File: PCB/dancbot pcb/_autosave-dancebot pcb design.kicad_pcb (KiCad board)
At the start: 2 copper layers, 62 x 54 mm, 27 parts, among them J1 ESP32-PICO-KIT-V4.1, J2 Voltage Regulator, J4 Pins, J6 Conn_01x04_Socket, J7 Conn_01x04_Socket, Q1 PMOS, Q2 PMOS, Q3 2N3904, Q5 PMOS, SW1 SP switch, SW2 SW_SPST

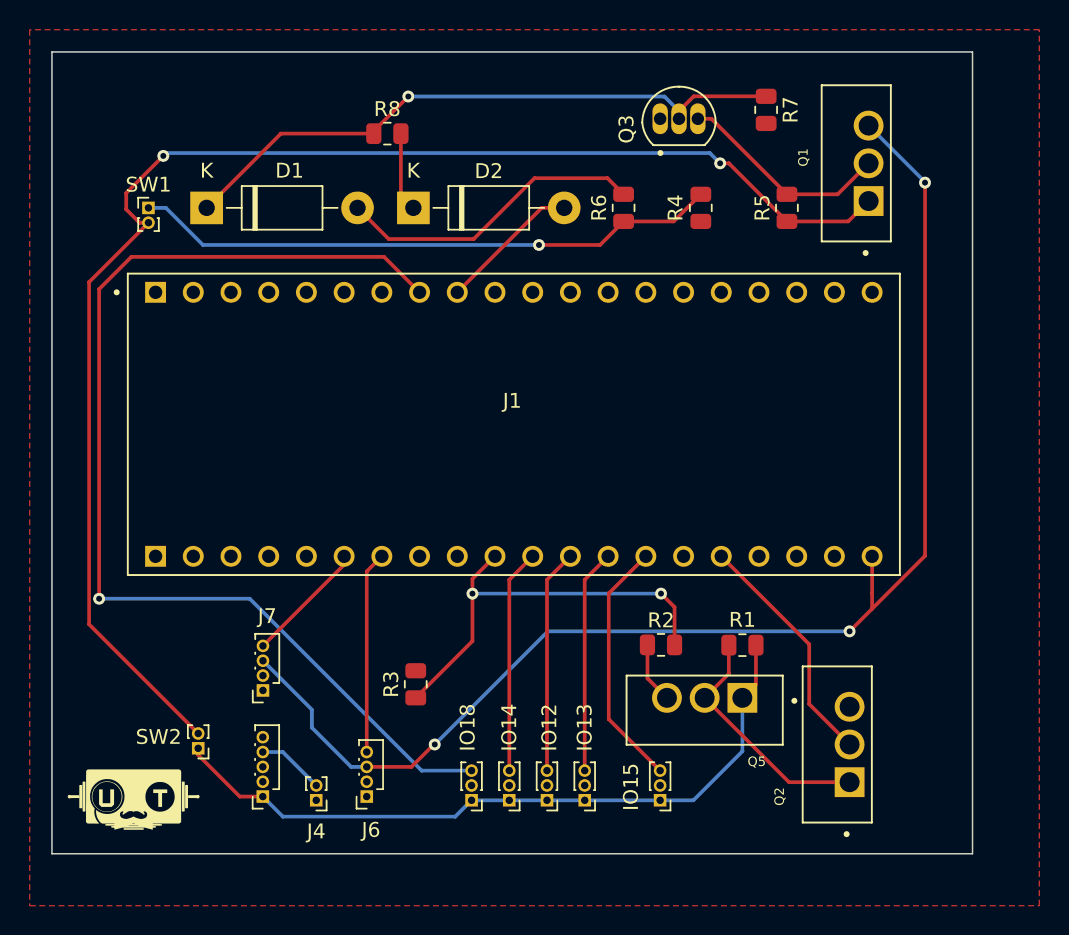
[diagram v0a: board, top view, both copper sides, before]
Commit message: Routing rev 6, trace width increased, smd components added
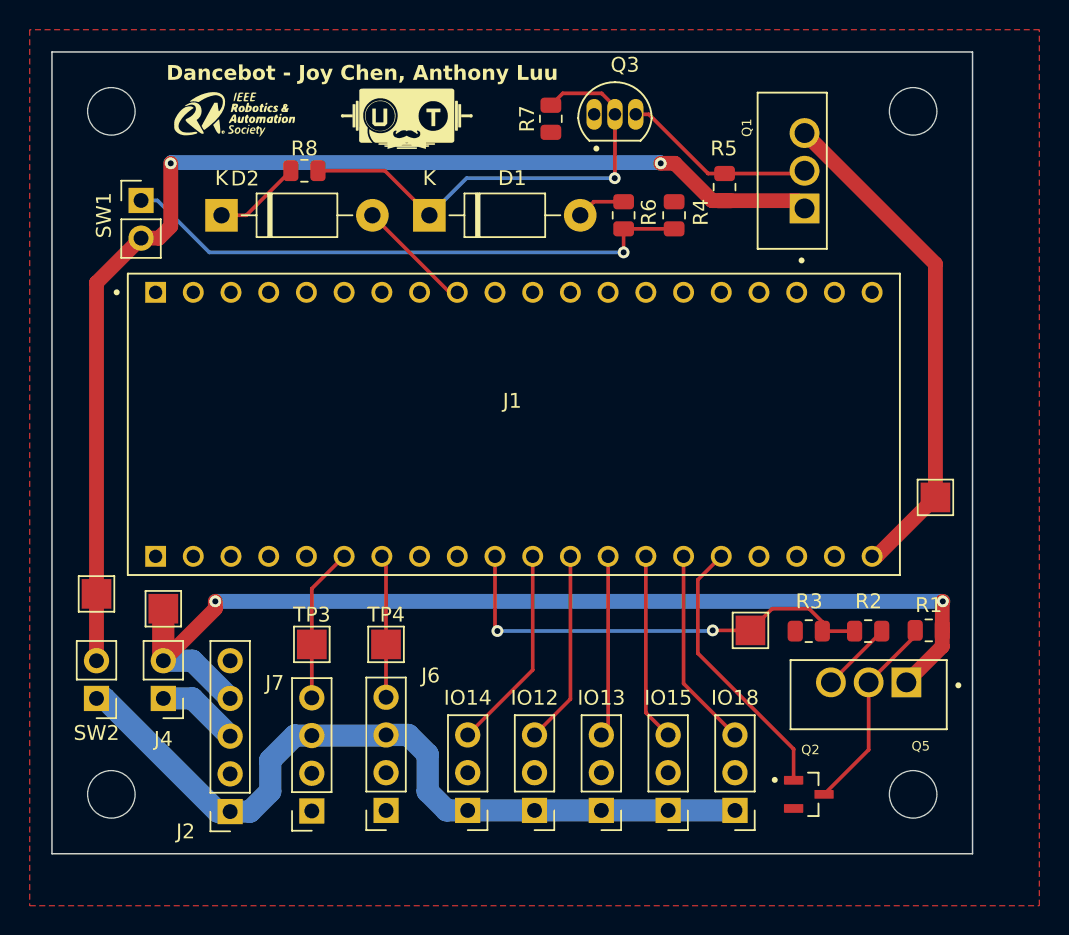
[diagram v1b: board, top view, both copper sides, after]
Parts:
- added G***: LOGO, LOGO, F.Cu at (194.8, 61.7)
- added H1: MountingHole, MountingHole:MountingHole_3.2mm_M3, F.Cu at (186.5, 61.5)
- added H2: MountingHole, MountingHole:MountingHole_3.2mm_M3, F.Cu at (240.5, 61.5)
- added H3: MountingHole, MountingHole:MountingHole_3.2mm_M3, F.Cu at (186.5, 107.5)
- added H4: MountingHole, MountingHole:MountingHole_3.2mm_M3, F.Cu at (240.5, 107.5)
- added TP1: TestPoint, TestPoint:TestPoint_Pad_2.0x2.0mm, F.Cu at (185.5, 94.0)
- added TP2: TestPoint, TestPoint:TestPoint_Pad_2.0x2.0mm, F.Cu at (242.0, 87.5)
- added TP3: TestPoint, TestPoint:TestPoint_Pad_2.0x2.0mm, F.Cu at (200.0, 97.4)
- added TP4: TestPoint, TestPoint:TestPoint_Pad_2.0x2.0mm, F.Cu at (205.0, 97.4)
- added TP5: TestPoint, TestPoint:TestPoint_Pad_2.0x2.0mm, F.Cu at (190.0, 95.0)
- added TP9: TestPoint, TestPoint:TestPoint_Pad_2.0x2.0mm, F.Cu at (229.5, 96.5)
- IO12, IO13, IO14, IO15, IO18: footprint Connector_PinHeader_1.00mm:PinHeader_1x03_P1.00mm_Vertical -> Connector_PinHeader_2.54mm:PinHeader_1x03_P2.54mm_Vertical
- J2: footprint Connector_PinSocket_1.00mm:PinSocket_1x05_P1.00mm_Vertical -> Connector_PinSocket_2.54mm:PinSocket_1x05_P2.54mm_Vertical
- J4, SW1, SW2: footprint Connector_PinHeader_1.00mm:PinHeader_1x02_P1.00mm_Vertical -> Connector_PinHeader_2.54mm:PinHeader_1x02_P2.54mm_Vertical
- J6, J7: footprint Connector_PinSocket_1.00mm:PinSocket_1x04_P1.00mm_Vertical -> Connector_PinSocket_2.54mm:PinSocket_1x04_P2.54mm_Vertical
- Q2: value PMOS -> NMOS; footprint dancebot pcb libraries stuff:TO254P1052X465X1989-3 -> Dancebot Footprints:SOT95P237X112-3N
- Q3: footprint 2N3904:TO92127P495H495-3 -> Dancebot Footprints:TO92127P495H495-3
- Q5: footprint dancebot pcb libraries stuff:TO254P1052X465X1989-3 -> Dancebot Footprints:TO254P1052X465X1989-3
- R3: value 10K -> 51k
- moved G*** 49.4 mm to (206.4, 61.6)
- moved R3 26.7 mm to (233.5, 96.5), turned to 180 degrees
- moved IO18 17.8 mm to (228.5, 108.6)
- moved D1 15.0 mm to (207.9, 68.5)
- moved R7 14.5 mm to (216.1, 62.0)
- moved R2 14.0 mm to (237.5, 96.5), turned to 180 degrees
- moved D2 12.9 mm to (193.9, 68.5)
- moved R1 12.6 mm to (241.6, 96.5)
- moved J4 12.4 mm to (190.0, 101.0)
- moved Q5 11.1 mm to (240.0, 100.0)
- moved J7 8.76 mm to (200.0, 108.6)
- moved SW2 7.63 mm to (185.5, 101.0)
- moved R8 6.12 mm to (199.5, 65.5), turned to 180 degrees
- moved R5 4.43 mm to (227.8, 66.6)
- moved Q1 4.34 mm to (233.2, 68.0)
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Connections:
- J1 pad J2_8: SM5 -> unconnected-(J1-IO18-PadJ2_8)
- J1 pad J3_15: unconnected-(J1-IO2-PadJ3_15) -> SM5
- J4 pad 1: GND1 -> Batt GND
- J6 pad 3: +5V -> VOUT
- J7 pad 3: +5V -> VOUT
- Q2 pad 1: Net-(Q2-D) -> BATT EN
- Q2 pad 2: BATT EN -> GND1
- Q2 pad 3: GND1 -> Net-(Q5-G)
- Q5 pad 1: VOUT -> Batt PWR
- Q5 pad 2: Net-(Q2-D) -> Net-(Q5-G)
- R1 pad 1: VOUT -> Batt PWR
- R1 pad 2: Net-(Q2-D) -> Net-(Q5-G)
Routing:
- net Batt PWR: track 4.53 -> 70.0 mm, vias 0 -> 2
- net SM5: track 74.2 -> 13.5 mm, vias 1 -> 0
- net +5V: track 88.3 -> 34.4 mm, vias 3 -> 0
- net Net-(D1-A): track 20.9 -> 3.30 mm
- net Net-(Q2-D): track 16.3 -> 0.00 mm
- net Net-(Q1-D): track 95.7 -> 80.3 mm
- net Net-(Q5-G): track 0.00 -> 13.6 mm
- net Net-(D1-K): track 42.8 -> 33.2 mm
- net Batt GND: track 0.00 -> 5.55 mm
- net SM4: track 16.9 -> 12.7 mm
- net NPRightEye: track 13.6 -> 9.61 mm
- net VOUT: track 49.4 -> 53.1 mm
- net SM3: track 15.1 -> 12.2 mm
- net NPLeftEye: track 8.30 -> 11.0 mm
- net BATT ADC: track 28.3 -> 30.8 mm
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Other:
- board text added: "Dancebot - Joy Chen, Anthony Luu"
